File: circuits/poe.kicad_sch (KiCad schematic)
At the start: 91 parts, among them J19 Conn_02x03_Odd_Even, J24 Conn_02x06_Odd_Even, Q15 Q_SI2325DS, Q16 Q_SI4848DY, Q17 SI7852DP, Q18 MMBTA06, Q19 MMBTA06, Q20 SI4850EY, T1 T_PA2649NL, U11 TL431, U2 TPS23754PWP-1, U4 OPTO-PC817

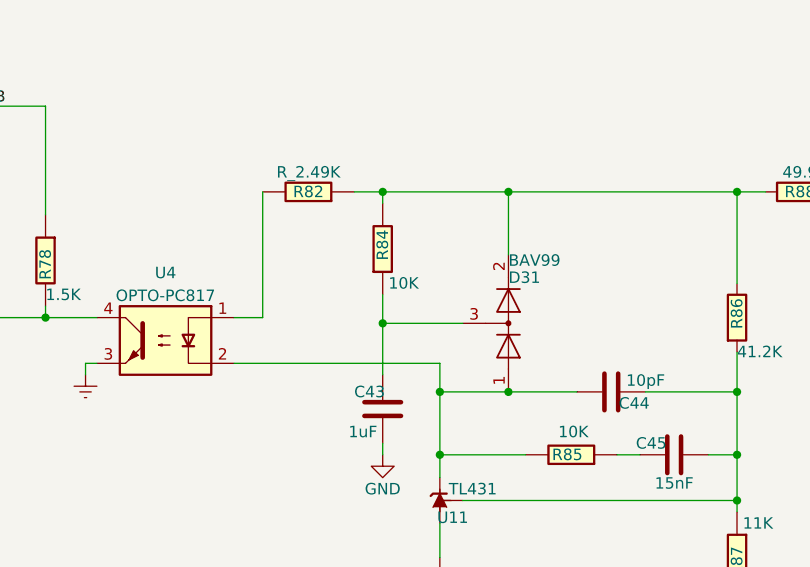
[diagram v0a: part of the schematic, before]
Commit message: corrected footprints for manufacturer
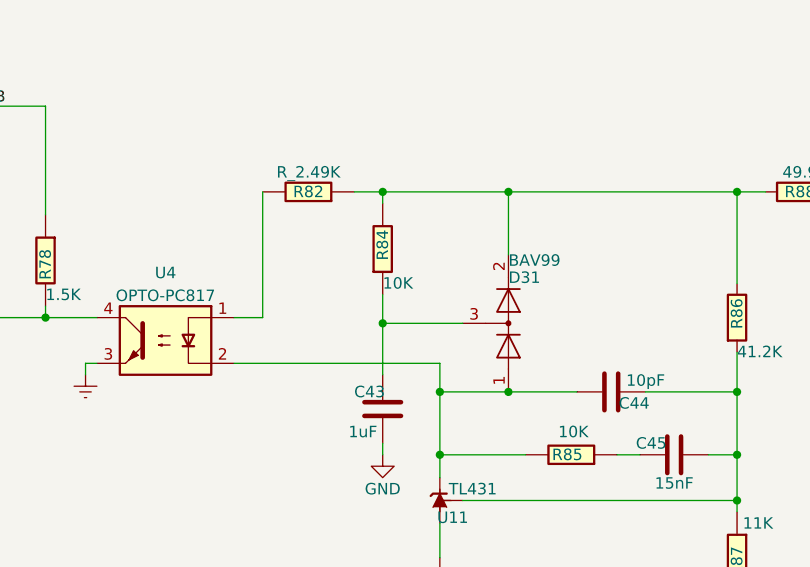
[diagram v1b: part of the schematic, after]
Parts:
- U11: footprint Package_SO:SOIC-8_3.9x4.9mm_P1.27mm -> Package_TO_SOT_SMD:SOT-23-5
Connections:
- net GND: now also U11.5 (A); no longer U11.2 (A), U11.3 (A), U11.6 (A), U11.7 (A)
- net at C44.2, C45.2, R86.2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: now also U11.4 (REF); no longer U11.8 (REF)
- net at C44.1, D31.1 (K), R85.2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: now also U11.3 (K); no longer U11.1 (K)
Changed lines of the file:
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@@
       (effects (font (size 1.27 1.27)) (justify left))
     )
-    (property "Value" "10K" (id 1) (at 283.845 196.85 0)
+    (property "Value" "10K" (id 1) (at 283.21 196.85 0)
       (effects (font (size 1.27 1.27)) (justify left))
     )
@@
       (effects (font (size 1.27 1.27)) (justify right))
     )
-    (property "Footprint" "Package_SO:SOIC-8_3.9x4.9mm_P1.27mm" (id 2) (at 302.26 220.98 0)
+    (property "Footprint" "Package_TO_SOT_SMD:SOT-23-5" (id 2) (at 302.26 220.98 0)
       (effects (font (size 1.27 1.27) italic) hide)
     )
@@
     (pin "1")
     (pin "2")
-    (pin "3")
     (pin "3")
     (pin "4")
     (pin "5")
-    (pin "6")
-    (pin "6")
-    (pin "7")
-    (pin "7")
-    (pin "8")
   )
 )

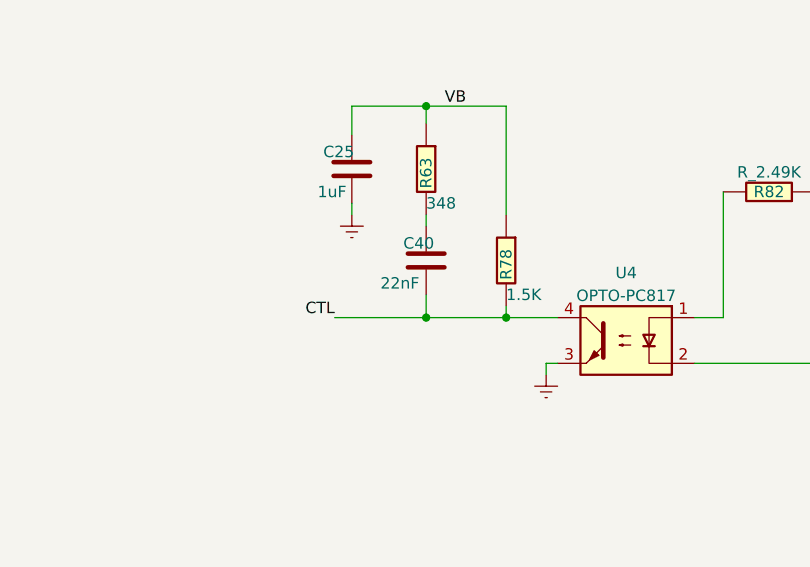
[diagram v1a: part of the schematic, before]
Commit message: Finished schematic for shrinking PCB for residential systems
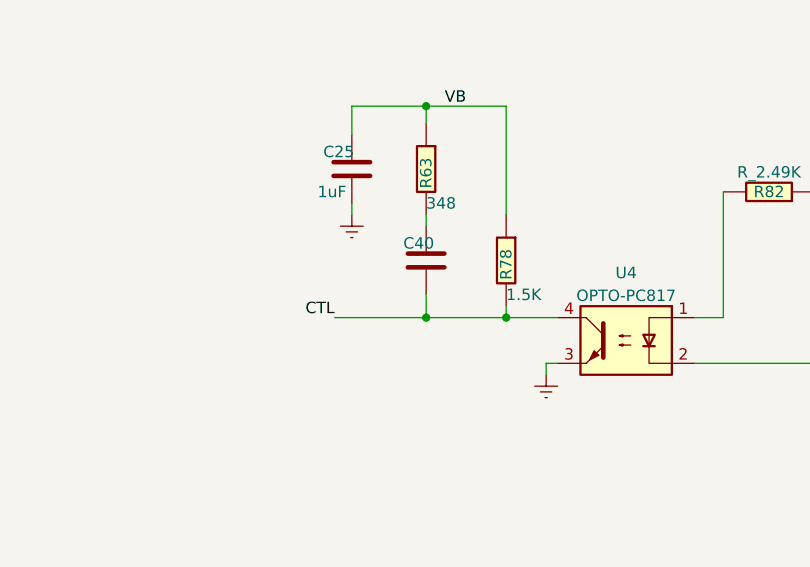
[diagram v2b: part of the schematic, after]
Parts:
- C40: value 22nF -> (none); LCSC C21122 -> C1532; Part Number CL10B223KB8NNNC -> 0402B223K500NT
- C41: footprint Capacitor_SMD:C_0603_1608Metric_Pad1.08x0.95mm_HandSolder -> Capacitor_SMD:C_0402_1005Metric
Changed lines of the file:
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@@
       (effects (font (size 1.27 1.27)) (justify left))
     )
-    (property "Value" "22nF" (id 1) (at 231.775 196.85 0)
+    (property "Value" "" (id 1) (at 231.775 196.85 0)
       (effects (font (size 1.27 1.27)) (justify left))
     )
@@
       (effects (font (size 1.27 1.27)) hide)
     )
-    (property "Datasheet" "https://datasheet.lcsc.com/lcsc/1811101610_Samsung-Electro-Mechanics-CL10B223KB8NNNC_C21122.pdf" (id 3) (at 236.855 200.66 0)
-      (effects (font (size 1.27 1.27)) hide)
-    )
-    (property "LCSC" "C21122" (id 4) (at 236.855 184.15 0)
-      (effects (font (size 1.27 1.27)) hide)
-    )
-    (property "Part Number" "CL10B223KB8NNNC" (id 5) (at 240.03 189.23 0)
+    (property "Datasheet" "https://datasheet.lcsc.com/lcsc/1811141710_FH-Guangdong-Fenghua-Advanced-Tech-0402B223K500NT_C1532.pdf" (id 3) (at 236.855 200.66 0)
+      (effects (font (size 1.27 1.27)) hide)
+    )
+    (property "LCSC" "C1532" (id 4) (at 236.855 184.15 0)
+      (effects (font (size 1.27 1.27)) hide)
+    )
+    (property "Part Number" "0402B223K500NT" (id 5) (at 240.03 189.23 0)
       (effects (font (size 1.524 1.524)) hide)
     )
@@
       (effects (font (size 1.27 1.27)) (justify left))
     )
-    (property "Footprint" "Capacitor_SMD:C_0603_1608Metric_Pad1.08x0.95mm_HandSolder" (id 2) (at 257.81 97.155 0)
-      (effects (font (size 1.27 1.27)) hide)
-    )
+    (property "Footprint" "Capacitor_SMD:C_0402_1005Metric" (id 2) (at 257.81 97.155 0)
+      (effects (font (size 1.27 1.27)) hide)
+    )
